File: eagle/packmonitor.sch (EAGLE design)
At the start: 7 parts, among them IC2 24C64, J1 UPDI_COMPACT

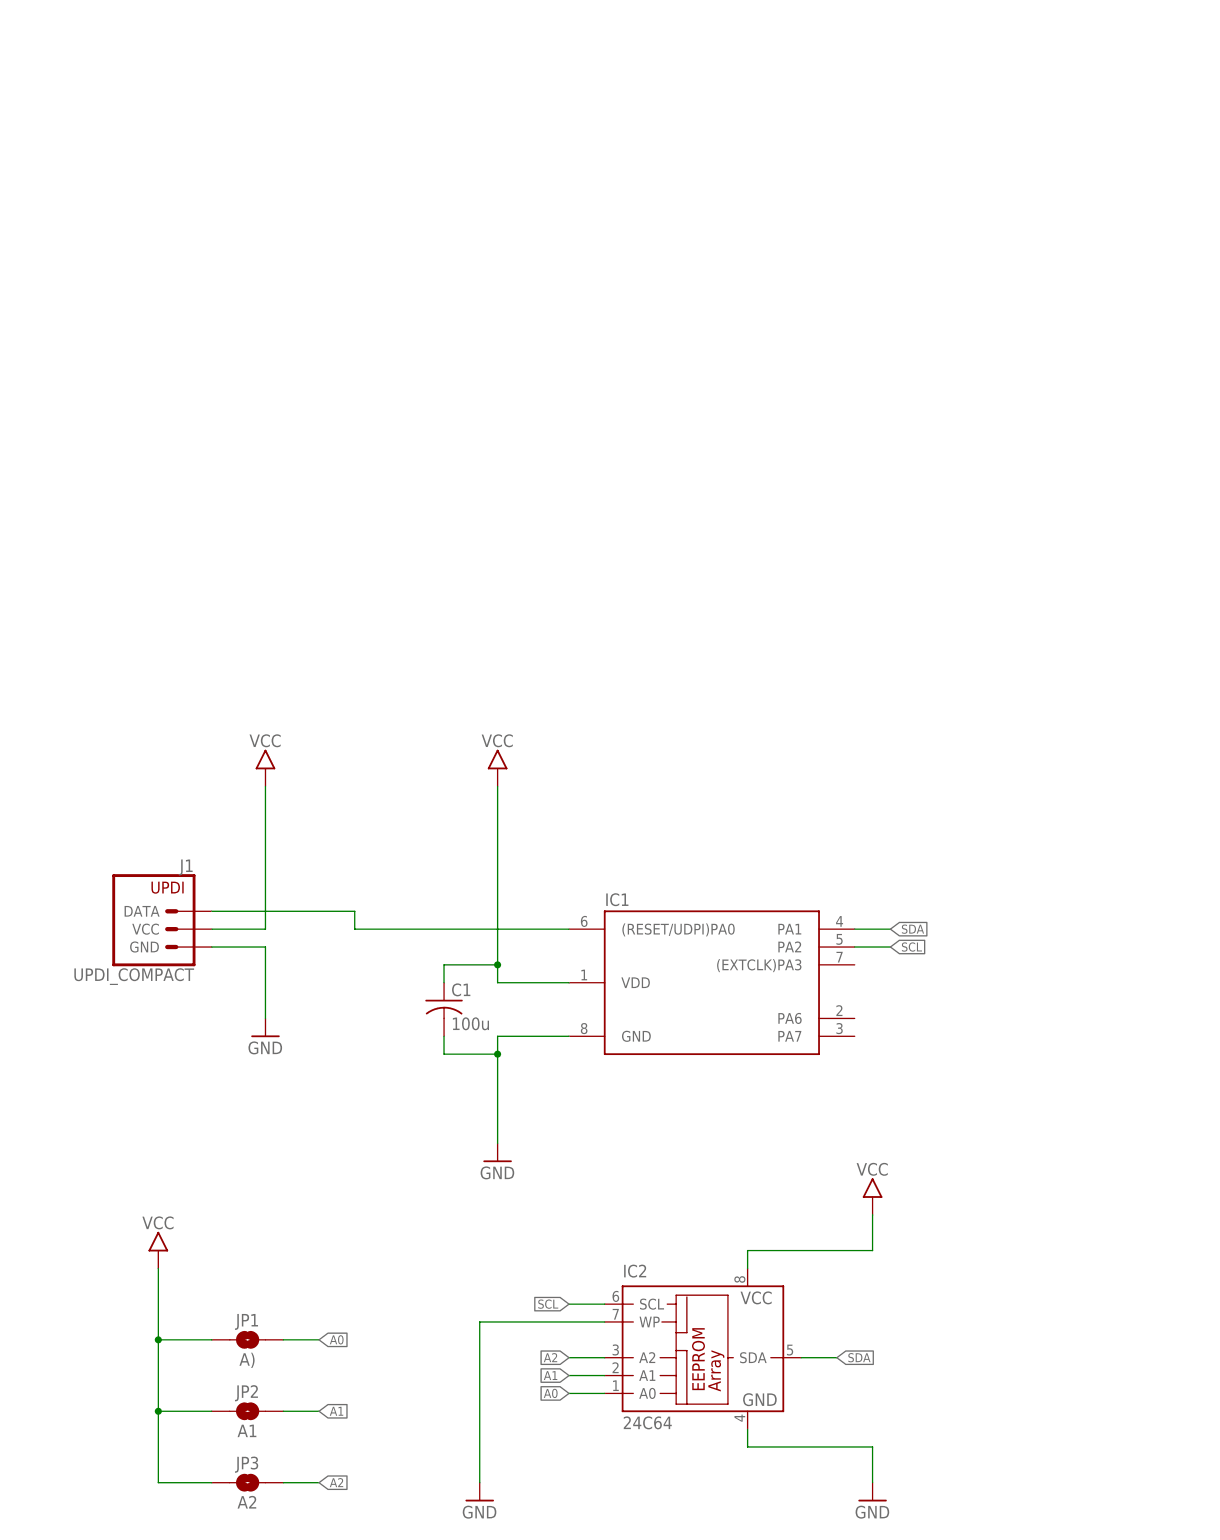
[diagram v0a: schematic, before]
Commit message: added 4808 mcu
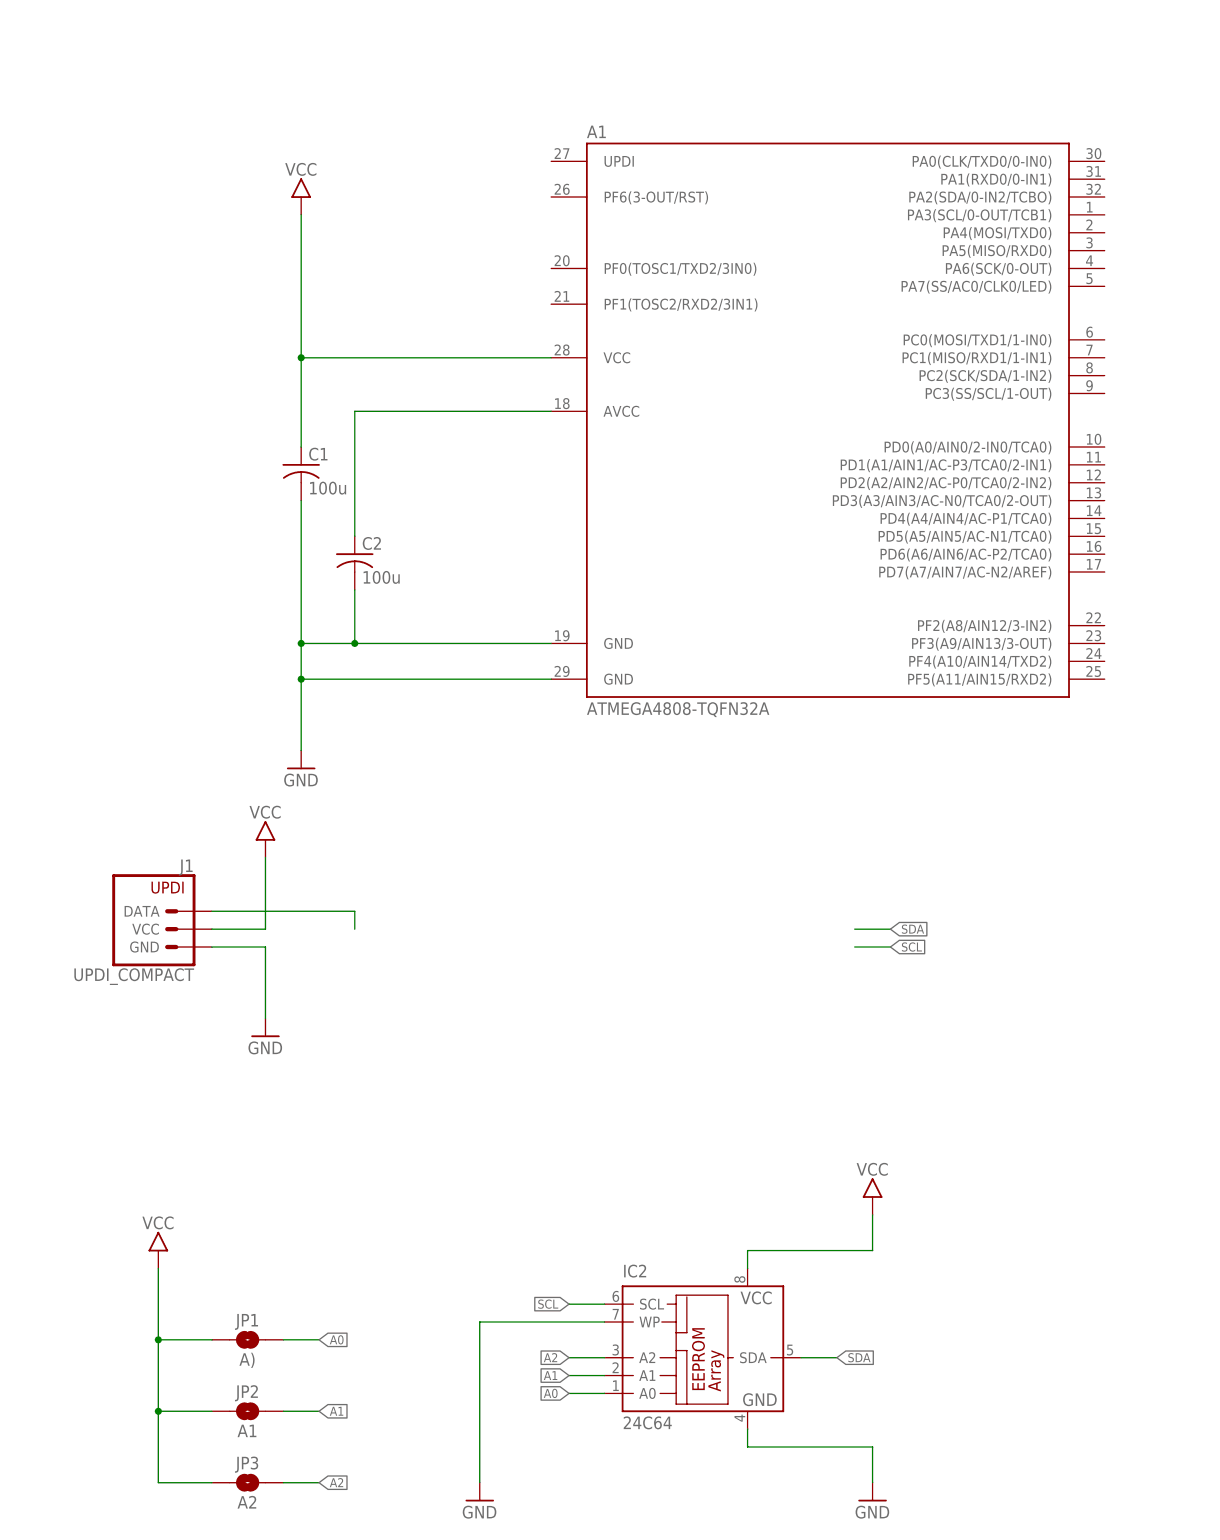
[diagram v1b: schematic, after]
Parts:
- removed IC1: (no value), bt_avr:ATTINY212/412
- added A1: ATMEGA4808-TQFN32A, microchip-special:ATMEGA4808-TQFN32A
- added C2: 100u, rcl:C-USC0603
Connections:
- new net N$2: A1.AVCC, C2.1
- net GND: now also A1.GND@1, A1.GND@2, C2.2; no longer IC1.GND
- net N$1: no longer IC1.(RESET/UDPI)PA0
- net SCL: no longer IC1.PA2
- net SDA: no longer IC1.PA1
- net VCC: now also A1.VCC; no longer IC1.VDD
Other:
- moved on the sheet: C1
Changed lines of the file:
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@@
 </classes>
 <parts>
-<part name="IC1" library="bt_avr" deviceset="ATTINY212/412" device=""/>
 <part name="J1" library="bt_avr" deviceset="UPDI" device="_COMPACT"/>
 <part name="U$1" library="bt" deviceset="VCC" device=""/>
@@
 <part name="JP3" library="SparkFun-Jumpers" deviceset="JUMPER-SMT_2_NO" device="_SILK" value="A2"/>
 <part name="U$4" library="bt" deviceset="VCC" device=""/>
+<part name="A1" library="microchip-special" deviceset="ATMEGA4808-TQFN32" device="A"/>
+<part name="C2" library="rcl" deviceset="C-US" device="C0603" value="100u"/>
 </parts>
 <sheets>
@@
 </plain>
 <instances>
-<instance part="IC1" gate="U1" x="50.8" y="68.58"/>
 <instance part="J1" gate="J1" x="-27.94" y="76.2" rot="MR0"/>
-<instance part="U$1" gate="G$1" x="-12.7" y="96.52"/>
-<instance part="U$2" gate="G$1" x="20.32" y="96.52"/>
+<instance part="U$1" gate="G$1" x="-12.7" y="86.36"/>
+<instance part="U$2" gate="G$1" x="-7.62" y="177.8"/>
 <instance part="GND1" gate="1" x="-12.7" y="60.96"/>
-<instance part="GND2" gate="1" x="20.32" y="43.18"/>
-<instance part="C1" gate="G$1" x="12.7" y="66.04"/>
+<instance part="GND2" gate="1" x="-7.62" y="99.06"/>
+<instance part="C1" gate="G$1" x="-7.62" y="142.24"/>
 <instance part="IC2" gate="G$1" x="48.26" y="15.24"/>
 <instance part="GND3" gate="1" x="73.66" y="-5.08"/>
@@
 <instance part="JP3" gate="G$1" x="-15.24" y="-2.54"/>
 <instance part="U$4" gate="G$1" x="-27.94" y="27.94"/>
+<instance part="A1" gate="G$1" x="68.58" y="149.86"/>
+<instance part="C2" gate="G$1" x="0" y="129.54"/>
 </instances>
 <busses>
@@
 <wire x1="-20.32" y1="78.74" x2="0" y2="78.74" width="0.1524" layer="91"/>
 <wire x1="0" y1="78.74" x2="0" y2="76.2" width="0.1524" layer="91"/>
-<pinref part="IC1" gate="U1" pin="(RESET/UDPI)PA0"/>
-<wire x1="0" y1="76.2" x2="30.48" y2="76.2" width="0.1524" layer="91"/>
 </segment>
 </net>
@@
 <pinref part="U$1" gate="G$1" pin="VCC"/>
 <wire x1="-20.32" y1="76.2" x2="-12.7" y2="76.2" width="0.1524" layer="91"/>
-<wire x1="-12.7" y1="76.2" x2="-12.7" y2="96.52" width="0.1524" layer="91"/>
-</segment>
-<segment>
-<pinref part="IC1" gate="U1" pin="VDD"/>
-<pinref part="U$2" gate="G$1" pin="VCC"/>
-<wire x1="30.48" y1="68.58" x2="20.32" y2="68.58" width="0.1524" layer="91"/>
-<wire x1="20.32" y1="68.58" x2="20.32" y2="71.12" width="0.1524" layer="91"/>
-<pinref part="C1" gate="G$1" pin="1"/>
-<wire x1="20.32" y1="71.12" x2="20.32" y2="96.52" width="0.1524" layer="91"/>
-<wire x1="20.32" y1="71.12" x2="12.7" y2="71.12" width="0.1524" layer="91"/>
-<wire x1="12.7" y1="71.12" x2="12.7" y2="68.58" width="0.1524" layer="91"/>
-<junction x="20.32" y="71.12"/>
+<wire x1="-12.7" y1="76.2" x2="-12.7" y2="86.36" width="0.1524" layer="91"/>
 </segment>
 <segment>
@@
 <junction x="-27.94" y="7.62"/>
 </segment>
+<segment>
+<pinref part="A1" gate="G$1" pin="VCC"/>
+<pinref part="U$2" gate="G$1" pin="VCC"/>
+<wire x1="27.94" y1="157.48" x2="-7.62" y2="157.48" width="0.1524" layer="91"/>
+<wire x1="-7.62" y1="157.48" x2="-7.62" y2="177.8" width="0.1524" layer="91"/>
+<pinref part="C1" gate="G$1" pin="1"/>
+<wire x1="-7.62" y1="157.48" x2="-7.62" y2="144.78" width="0.1524" layer="91"/>
+<junction x="-7.62" y="157.48"/>
+</segment>
 </net>
 <net name="GND" class="0">
-<segment>
-<pinref part="IC1" gate="U1" pin="GND"/>
-<pinref part="GND2" gate="1" pin="GND"/>
-<wire x1="30.48" y1="60.96" x2="20.32" y2="60.96" width="0.1524" layer="91"/>
-<wire x1="20.32" y1="60.96" x2="20.32" y2="58.42" width="0.1524" layer="91"/>
-<pinref part="C1" gate="G$1" pin="2"/>
-<wire x1="20.32" y1="58.42" x2="20.32" y2="45.72" width="0.1524" layer="91"/>
-<wire x1="12.7" y1="60.96" x2="12.7" y2="58.42" width="0.1524" layer="91"/>
-<wire x1="12.7" y1="58.42" x2="20.32" y2="58.42" width="0.1524" layer="91"/>
-<junction x="20.32" y="58.42"/>
-</segment>
 <segment>
 <pinref part="J1" gate="J1" pin="GND"/>
@@
 <wire x1="35.56" y1="20.32" x2="17.78" y2="20.32" width="0.1524" layer="91"/>
 <wire x1="17.78" y1="20.32" x2="17.78" y2="-2.54" width="0.1524" layer="91"/>
+</segment>
+<segment>
+<pinref part="C1" gate="G$1" pin="2"/>
+<pinref part="GND2" gate="1" pin="GND"/>
+<wire x1="-7.62" y1="137.16" x2="-7.62" y2="116.84" width="0.1524" layer="91"/>
+<pinref part="A1" gate="G$1" pin="GND@2"/>
+<wire x1="-7.62" y1="116.84" x2="-7.62" y2="111.76" width="0.1524" layer="91"/>
+<wire x1="-7.62" y1="111.76" x2="-7.62" y2="101.6" width="0.1524" layer="91"/>
+<wire x1="27.94" y1="111.76" x2="-7.62" y2="111.76" width="0.1524" layer="91"/>
+<pinref part="A1" gate="G$1" pin="GND@1"/>
+<wire x1="27.94" y1="116.84" x2="0" y2="116.84" width="0.1524" layer="91"/>
+<junction x="-7.62" y="116.84"/>
+<junction x="-7.62" y="111.76"/>
+<pinref part="C2" gate="G$1" pin="2"/>
+<wire x1="0" y1="116.84" x2="-7.62" y2="116.84" width="0.1524" layer="91"/>
+<wire x1="0" y1="124.46" x2="0" y2="116.84" width="0.1524" layer="91"/>
+<junction x="0" y="116.84"/>
 </segment>
 </net>
@@
 <net name="SDA" class="0">
 <segment>
-<pinref part="IC1" gate="U1" pin="PA1"/>
 <wire x1="76.2" y1="76.2" x2="71.12" y2="76.2" width="0.1524" layer="91"/>
 <label x="76.2" y="76.2" size="1.27" layer="95" xref="yes"/>
@@
 <net name="SCL" class="0">
 <segment>
-<pinref part="IC1" gate="U1" pin="PA2"/>
 <wire x1="76.2" y1="73.66" x2="71.12" y2="73.66" width="0.1524" layer="91"/>
 <label x="76.2" y="73.66" size="1.27" layer="95" xref="yes"/>
@@
 </segment>
 </net>
+<net name="N$2" class="0">
+<segment>
+<pinref part="A1" gate="G$1" pin="AVCC"/>
+<pinref part="C2" gate="G$1" pin="1"/>
+<wire x1="27.94" y1="149.86" x2="0" y2="149.86" width="0.1524" layer="91"/>
+<wire x1="0" y1="149.86" x2="0" y2="132.08" width="0.1524" layer="91"/>
+</segment>
+</net>

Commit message: slowly adding parts and putting together layout
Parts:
- added C3: 100u, rcl:C-USC0603
- J1: value UPDI_COMPACT -> (none); device bt_avr:UPDI_COMPACT -> SparkFun-Connectors:M03LOCK_LONGPADS
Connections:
- removed net N$1: J1.DATA
- net GND: now also C3.2, J1.1; no longer J1.GND
- net N$2: now also A1.UPDI, J1.2; no longer A1.AVCC, C2.1
- net SCL: now also A1.PA3(SCL/0-OUT/TCB1)
- net SDA: now also A1.PA2(SDA/0-IN2/TCBO)
- net VCC: now also A1.AVCC, C2.1, C3.1, J1.3; no longer J1.VCC
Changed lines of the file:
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@@
 </classes>
 <parts>
-<part name="J1" library="bt_avr" deviceset="UPDI" device="_COMPACT"/>
-<part name="U$1" library="bt" deviceset="VCC" device=""/>
 <part name="U$2" library="bt" deviceset="VCC" device=""/>
-<part name="GND1" library="bt" deviceset="GND" device=""/>
 <part name="GND2" library="bt" deviceset="GND" device=""/>
 <part name="C1" library="rcl" deviceset="C-US" device="C0603" value="100u"/>
@@
 <part name="A1" library="microchip-special" deviceset="ATMEGA4808-TQFN32" device="A"/>
 <part name="C2" library="rcl" deviceset="C-US" device="C0603" value="100u"/>
+<part name="J1" library="SparkFun-Connectors" deviceset="M03" device="LOCK_LONGPADS"/>
+<part name="U$5" library="bt" deviceset="VCC" device=""/>
+<part name="GND4" library="bt" deviceset="GND" device=""/>
+<part name="C3" library="rcl" deviceset="C-US" device="C0603" value="100u"/>
 </parts>
 <sheets>
@@
 </plain>
 <instances>
-<instance part="J1" gate="J1" x="-27.94" y="76.2" rot="MR0"/>
-<instance part="U$1" gate="G$1" x="-12.7" y="86.36"/>
-<instance part="U$2" gate="G$1" x="-7.62" y="177.8"/>
-<instance part="GND1" gate="1" x="-12.7" y="60.96"/>
+<instance part="U$2" gate="G$1" x="-7.62" y="167.64"/>
 <instance part="GND2" gate="1" x="-7.62" y="99.06"/>
 <instance part="C1" gate="G$1" x="-7.62" y="142.24"/>
@@
 <instance part="A1" gate="G$1" x="68.58" y="149.86"/>
 <instance part="C2" gate="G$1" x="0" y="129.54"/>
+<instance part="J1" gate="J$1" x="-45.72" y="185.42"/>
+<instance part="U$5" gate="G$1" x="-30.48" y="198.12"/>
+<instance part="GND4" gate="1" x="-30.48" y="175.26"/>
+<instance part="C3" gate="G$1" x="81.28" y="17.78"/>
 </instances>
 <busses>
 </busses>
 <nets>
-<net name="N$1" class="0">
-<segment>
-<pinref part="J1" gate="J1" pin="DATA"/>
-<wire x1="-20.32" y1="78.74" x2="0" y2="78.74" width="0.1524" layer="91"/>
-<wire x1="0" y1="78.74" x2="0" y2="76.2" width="0.1524" layer="91"/>
-</segment>
-</net>
 <net name="VCC" class="0">
-<segment>
-<pinref part="J1" gate="J1" pin="VCC"/>
-<pinref part="U$1" gate="G$1" pin="VCC"/>
-<wire x1="-20.32" y1="76.2" x2="-12.7" y2="76.2" width="0.1524" layer="91"/>
-<wire x1="-12.7" y1="76.2" x2="-12.7" y2="86.36" width="0.1524" layer="91"/>
-</segment>
 <segment>
 <pinref part="IC2" gate="G$1" pin="VCC"/>
@@
 <wire x1="55.88" y1="30.48" x2="73.66" y2="30.48" width="0.1524" layer="91"/>
 <wire x1="73.66" y1="30.48" x2="73.66" y2="35.56" width="0.1524" layer="91"/>
+<pinref part="C3" gate="G$1" pin="1"/>
+<wire x1="73.66" y1="30.48" x2="81.28" y2="30.48" width="0.1524" layer="91"/>
+<wire x1="81.28" y1="30.48" x2="81.28" y2="20.32" width="0.1524" layer="91"/>
+<junction x="73.66" y="30.48"/>
 </segment>
 <segment>
@@
 <pinref part="A1" gate="G$1" pin="VCC"/>
 <pinref part="U$2" gate="G$1" pin="VCC"/>
-<wire x1="27.94" y1="157.48" x2="-7.62" y2="157.48" width="0.1524" layer="91"/>
-<wire x1="-7.62" y1="157.48" x2="-7.62" y2="177.8" width="0.1524" layer="91"/>
+<wire x1="27.94" y1="157.48" x2="0" y2="157.48" width="0.1524" layer="91"/>
+<wire x1="0" y1="157.48" x2="-7.62" y2="157.48" width="0.1524" layer="91"/>
+<wire x1="-7.62" y1="157.48" x2="-7.62" y2="167.64" width="0.1524" layer="91"/>
 <pinref part="C1" gate="G$1" pin="1"/>
 <wire x1="-7.62" y1="157.48" x2="-7.62" y2="144.78" width="0.1524" layer="91"/>
 <junction x="-7.62" y="157.48"/>
+<pinref part="A1" gate="G$1" pin="AVCC"/>
+<pinref part="C2" gate="G$1" pin="1"/>
+<wire x1="27.94" y1="149.86" x2="0" y2="149.86" width="0.1524" layer="91"/>
+<wire x1="0" y1="149.86" x2="0" y2="132.08" width="0.1524" layer="91"/>
+<wire x1="0" y1="149.86" x2="0" y2="157.48" width="0.1524" layer="91"/>
+<junction x="0" y="149.86"/>
+<junction x="0" y="157.48"/>
+</segment>
+<segment>
+<pinref part="J1" gate="J$1" pin="3"/>
+<pinref part="U$5" gate="G$1" pin="VCC"/>
+<wire x1="-38.1" y1="187.96" x2="-30.48" y2="187.96" width="0.1524" layer="91"/>
+<wire x1="-30.48" y1="187.96" x2="-30.48" y2="198.12" width="0.1524" layer="91"/>
 </segment>
 </net>
 <net name="GND" class="0">
-<segment>
-<pinref part="J1" gate="J1" pin="GND"/>
-<pinref part="GND1" gate="1" pin="GND"/>
-<wire x1="-20.32" y1="73.66" x2="-12.7" y2="73.66" width="0.1524" layer="91"/>
-<wire x1="-12.7" y1="73.66" x2="-12.7" y2="63.5" width="0.1524" layer="91"/>
-</segment>
 <segment>
 <pinref part="IC2" gate="G$1" pin="GND"/>
@@
 <wire x1="55.88" y1="2.54" x2="73.66" y2="2.54" width="0.1524" layer="91"/>
 <wire x1="73.66" y1="2.54" x2="73.66" y2="-2.54" width="0.1524" layer="91"/>
+<pinref part="C3" gate="G$1" pin="2"/>
+<wire x1="73.66" y1="2.54" x2="81.28" y2="2.54" width="0.1524" layer="91"/>
+<wire x1="81.28" y1="2.54" x2="81.28" y2="12.7" width="0.1524" layer="91"/>
+<junction x="73.66" y="2.54"/>
 </segment>
 <segment>
@@
 <junction x="0" y="116.84"/>
 </segment>
+<segment>
+<pinref part="J1" gate="J$1" pin="1"/>
+<pinref part="GND4" gate="1" pin="GND"/>
+<wire x1="-38.1" y1="182.88" x2="-30.48" y2="182.88" width="0.1524" layer="91"/>
+<wire x1="-30.48" y1="182.88" x2="-30.48" y2="177.8" width="0.1524" layer="91"/>
+</segment>
 </net>
 <net name="A0" class="0">
@@
 <label x="68.58" y="15.24" size="1.27" layer="95" xref="yes"/>
 </segment>
+<segment>
+<pinref part="A1" gate="G$1" pin="PA2(SDA/0-IN2/TCBO)"/>
+<wire x1="114.3" y1="180.34" x2="106.68" y2="180.34" width="0.1524" layer="91"/>
+<label x="114.3" y="180.34" size="1.27" layer="95" xref="yes"/>
+</segment>
 </net>
 <net name="SCL" class="0">
@@
 <label x="30.48" y="22.86" size="1.27" layer="95" rot="R180" xref="yes"/>
 </segment>
+<segment>
+<pinref part="A1" gate="G$1" pin="PA3(SCL/0-OUT/TCB1)"/>
+<wire x1="114.3" y1="177.8" x2="106.68" y2="177.8" width="0.1524" layer="91"/>
+<label x="114.3" y="177.8" size="1.27" layer="95" xref="yes"/>
+</segment>
 </net>
 <net name="N$2" class="0">
 <segment>
-<pinref part="A1" gate="G$1" pin="AVCC"/>
-<pinref part="C2" gate="G$1" pin="1"/>
-<wire x1="27.94" y1="149.86" x2="0" y2="149.86" width="0.1524" layer="91"/>
-<wire x1="0" y1="149.86" x2="0" y2="132.08" width="0.1524" layer="91"/>
-</segment>
-</net>
+<pinref part="J1" gate="J$1" pin="2"/>
+<pinref part="A1" gate="G$1" pin="UPDI"/>
+<wire x1="-38.1" y1="185.42" x2="27.94" y2="185.42" width="0.1524" layer="91"/>
+</segment>
+</net>
